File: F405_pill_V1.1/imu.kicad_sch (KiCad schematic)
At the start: 22 parts, among them U6 BMI160, U7 MPU-9250, U8 LSM6DS3, U9 ICM-20948

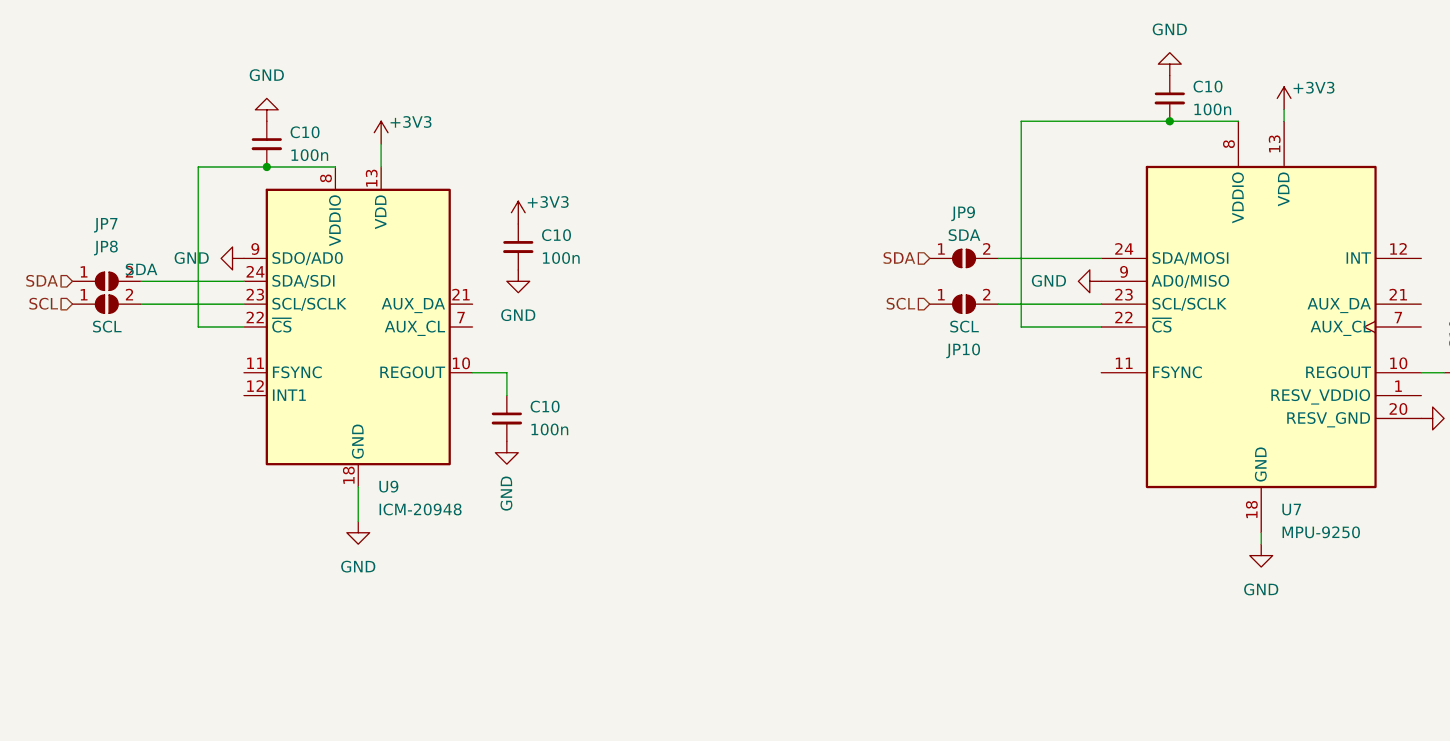
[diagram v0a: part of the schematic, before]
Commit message: removed one imu
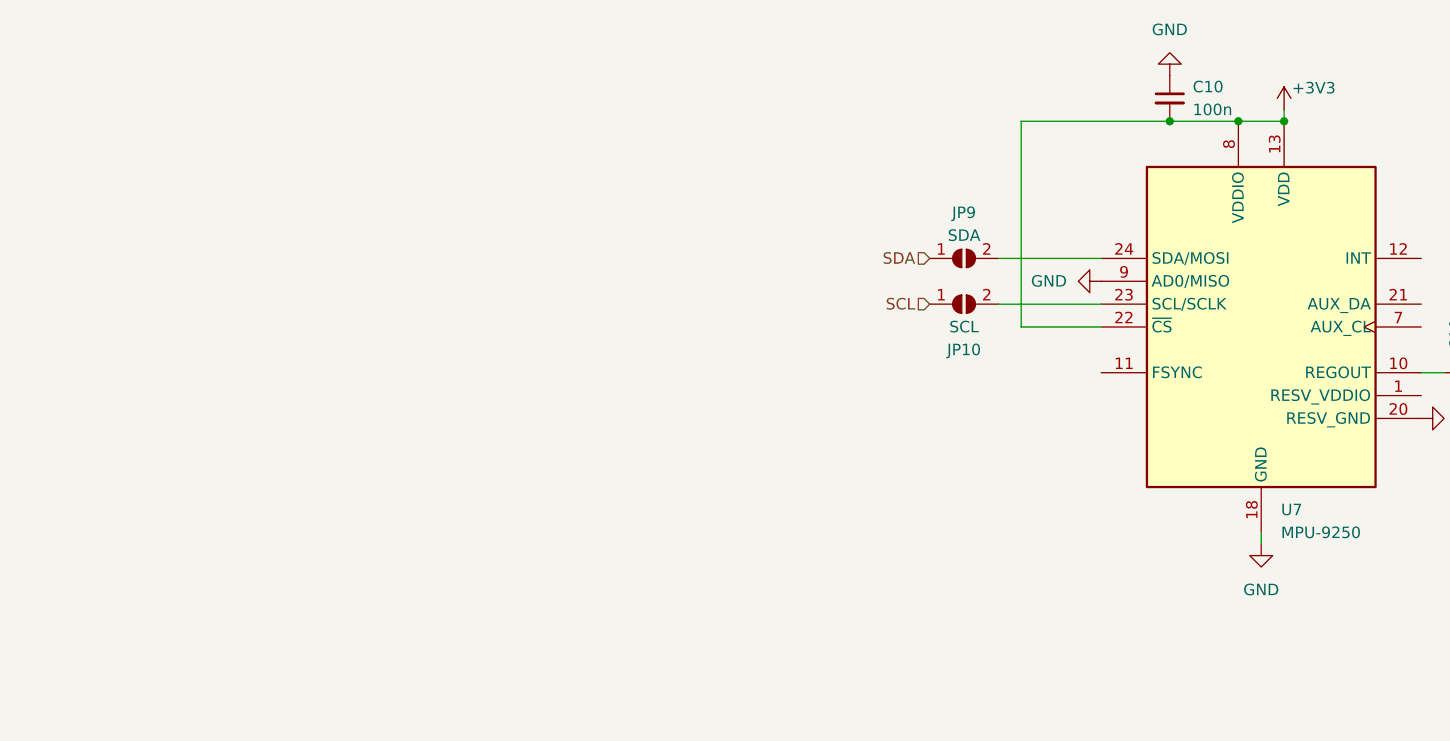
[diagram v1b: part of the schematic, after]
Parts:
- removed C10 (x3): 100n, Capacitor_SMD:C_0402_1005Metric, symbol Device:C_Small
- removed JP7: SDA, Jumper:SolderJumper-2_P1.3mm_Open_RoundedPad1.0x1.5mm, symbol Jumper:SolderJumper_2_Open
- removed JP8: SCL, Jumper:SolderJumper-2_P1.3mm_Open_RoundedPad1.0x1.5mm, symbol Jumper:SolderJumper_2_Open
- removed U9: ICM-20948, Sensor_Motion:InvenSense_QFN-24_3x3mm_P0.4mm, symbol Sensor_Motion:ICM-20948
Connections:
- net +3V3: now also C10.2, U7.22 (~{CS}), U7.8 (VDDIO)

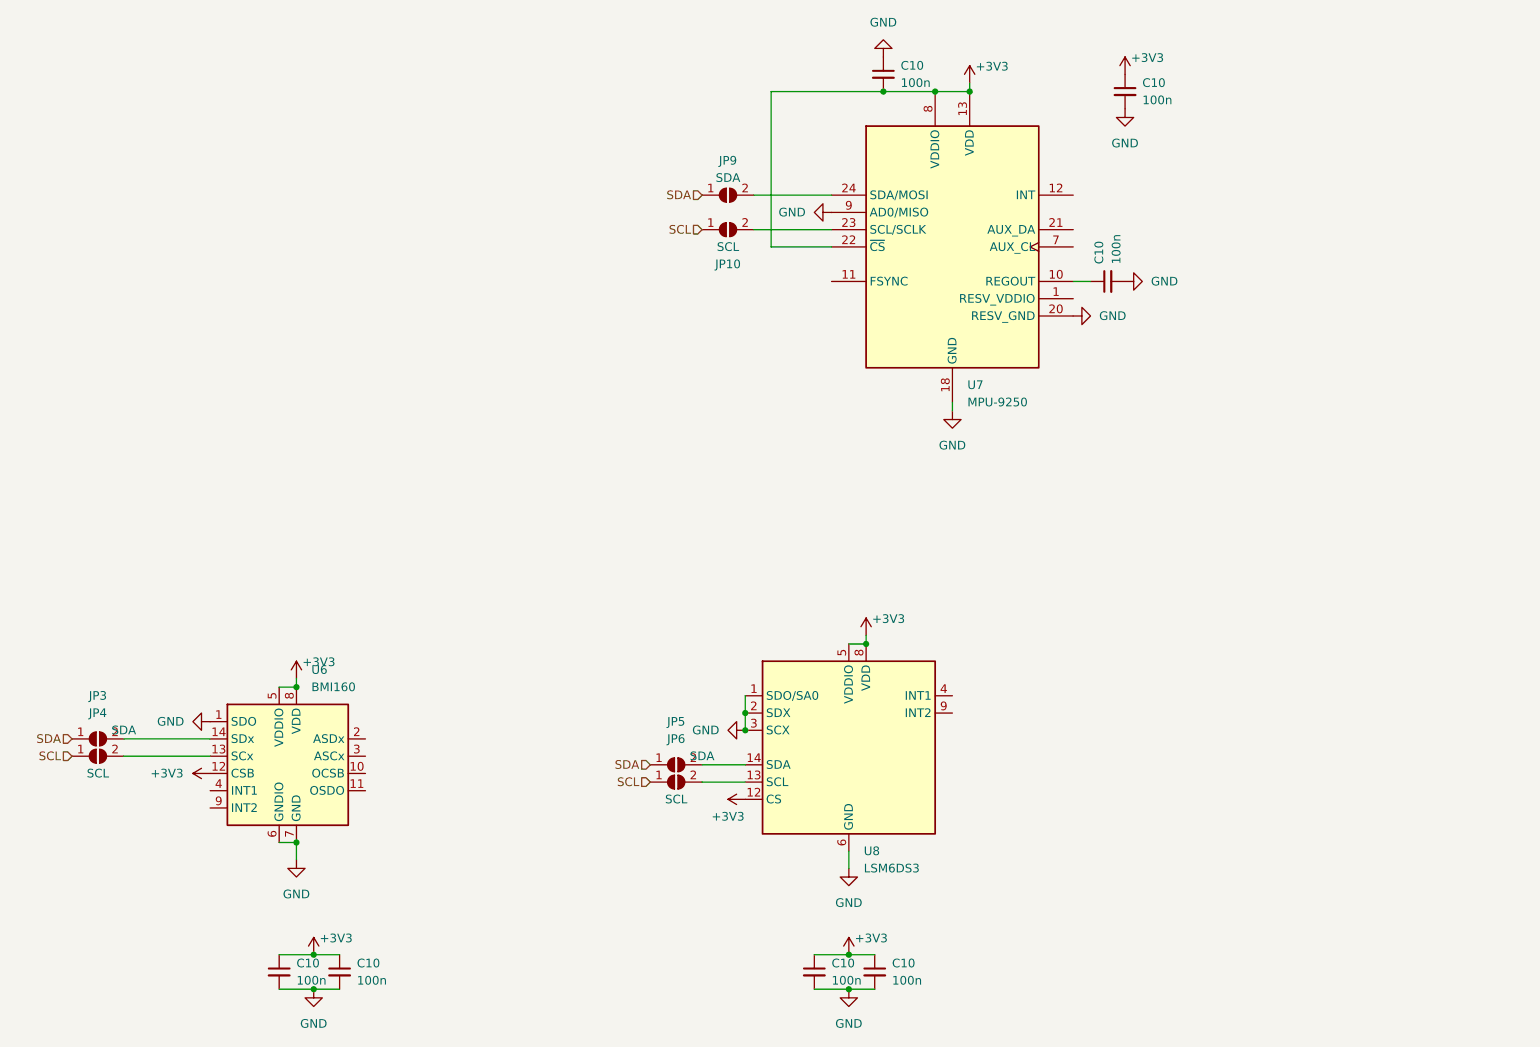
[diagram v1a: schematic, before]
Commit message: add bmi270
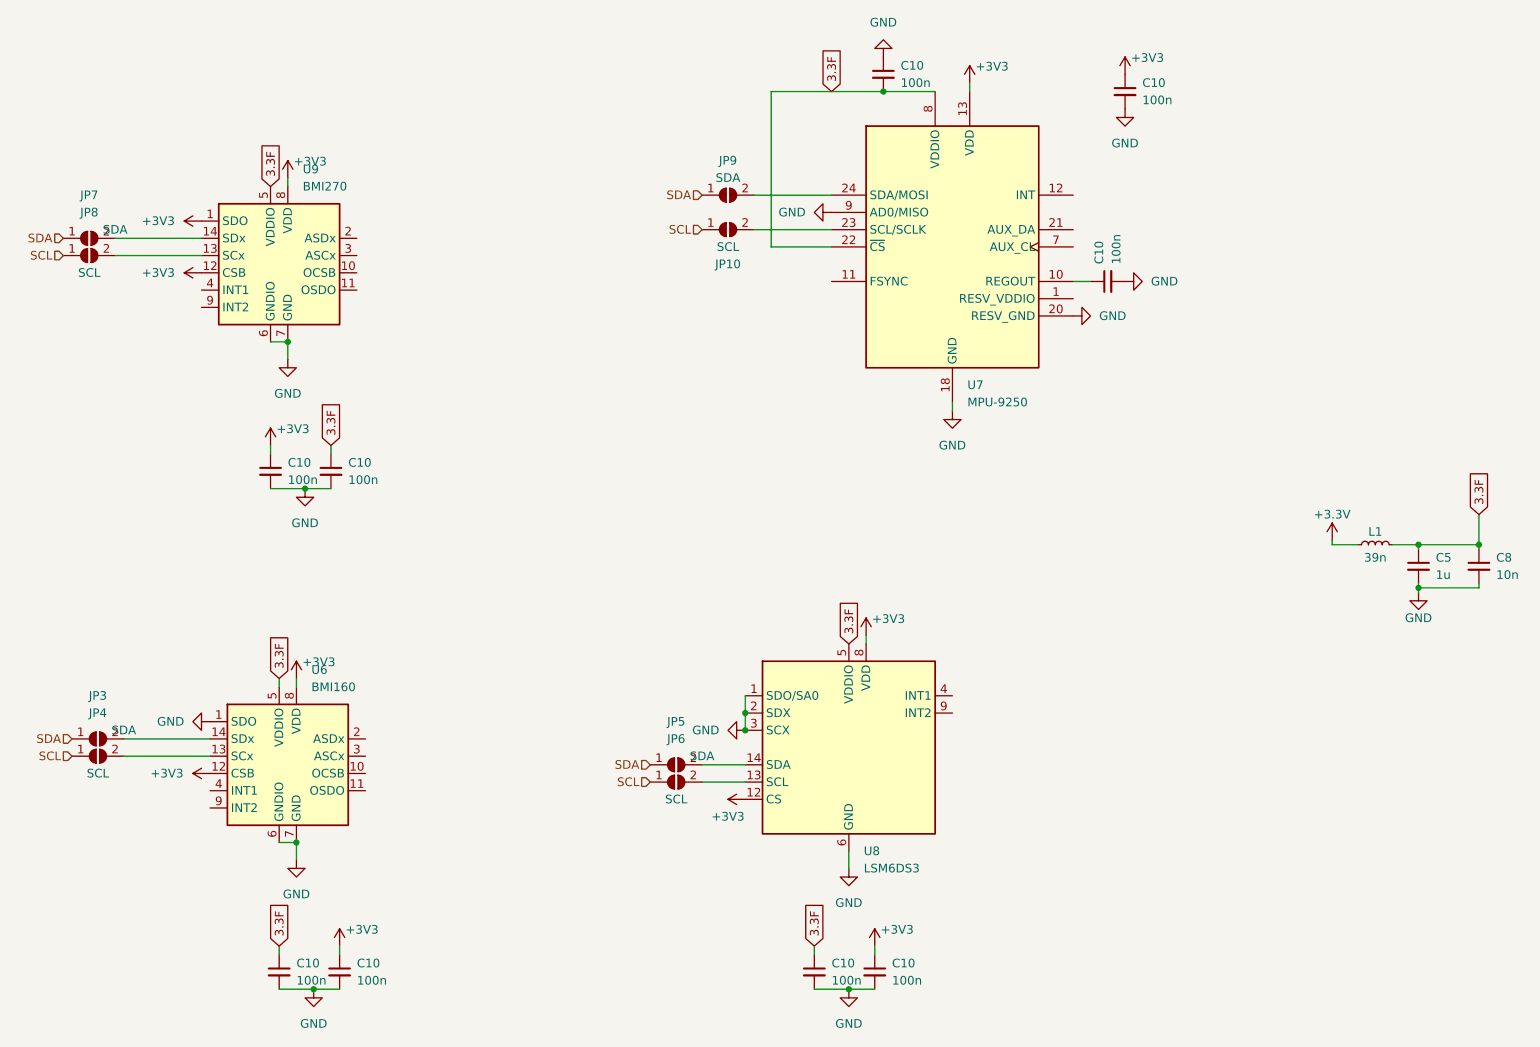
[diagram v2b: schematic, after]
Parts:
- added C10 (x2): 100n, Capacitor_SMD:C_0402_1005Metric, symbol Device:C_Small
- added C5: 1u, Capacitor_SMD:C_0402_1005Metric, symbol Device:C_Small
- added C8: 10n, Capacitor_SMD:C_0402_1005Metric, symbol Device:C_Small
- added JP7: SDA, Jumper:SolderJumper-2_P1.3mm_Open_RoundedPad1.0x1.5mm, symbol Jumper:SolderJumper_2_Open
- added JP8: SCL, Jumper:SolderJumper-2_P1.3mm_Open_RoundedPad1.0x1.5mm, symbol Jumper:SolderJumper_2_Open
- added L1: 39n, Inductor_SMD:L_0402_1005Metric, symbol Device:L_Small
- added U9: BMI270, Package_LGA:Bosch_LGA-14_3x2.5mm_P0.5mm, symbol Sensor_Motion:BMI160
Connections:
- net +3V3: now also C10.1, L1.1, U9.1 (SDO), U9.12 (CSB), U9.8 (VDD); no longer C10.1, C10.1, C10.2, U6.5 (VDDIO), U7.22 (~{CS}), U7.8 (VDDIO), U8.5 (VDDIO)
- net GND: now also C10.2, C10.2, C5.2, C8.2, U9.6 (GNDIO), U9.7 (GND)
- net SCL: now also JP8.1 (A)
- net SDA: now also JP7.1 (A)
- new net: JP7.2 (B), U9.14 (SDx)
- new net: JP8.2 (B), U9.13 (SCx)
- new net 3.3F: C10.1, C10.1, C10.1, C10.2, C5.1, C8.1, L1.2, U6.5 (VDDIO), U7.22 (~{CS}), U7.8 (VDDIO), U8.5 (VDDIO), U9.5 (VDDIO)

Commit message: add MCU
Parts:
- removed C10 (x7): 100n, Capacitor_SMD:C_0402_1005Metric, symbol Device:C_Small
- removed JP10, JP4, JP6, JP8: SCL, Jumper:SolderJumper-2_P1.3mm_Open_RoundedPad1.0x1.5mm, symbol Jumper:SolderJumper_2_Open
- removed JP3, JP5, JP7, JP9: SDA, Jumper:SolderJumper-2_P1.3mm_Open_RoundedPad1.0x1.5mm, symbol Jumper:SolderJumper_2_Open
- removed U6: BMI160, Package_LGA:Bosch_LGA-14_3x2.5mm_P0.5mm, symbol Sensor_Motion:BMI160
- removed U7: MPU-9250, Sensor_Motion:InvenSense_QFN-24_3x3mm_P0.4mm, symbol Sensor_Motion:MPU-9250
- removed U9: BMI270, Package_LGA:Bosch_LGA-14_3x2.5mm_P0.5mm, symbol Sensor_Motion:BMI160
- renumbered C10 to C28, C10 to C29, C5 to C30, C8 to C31, L1 to L2
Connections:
- net SCL: now also U8.13 (SCL)
- net SDA: now also U8.14 (SDA)
